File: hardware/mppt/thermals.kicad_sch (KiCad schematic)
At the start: 35 parts, among them J401 Conn_01x02, J402 Conn_01x03, J403 Conn_01x03, J404 Conn_01x03, Q401 Q_NMOS_GDS, U401 MCP9700Ax-ELT

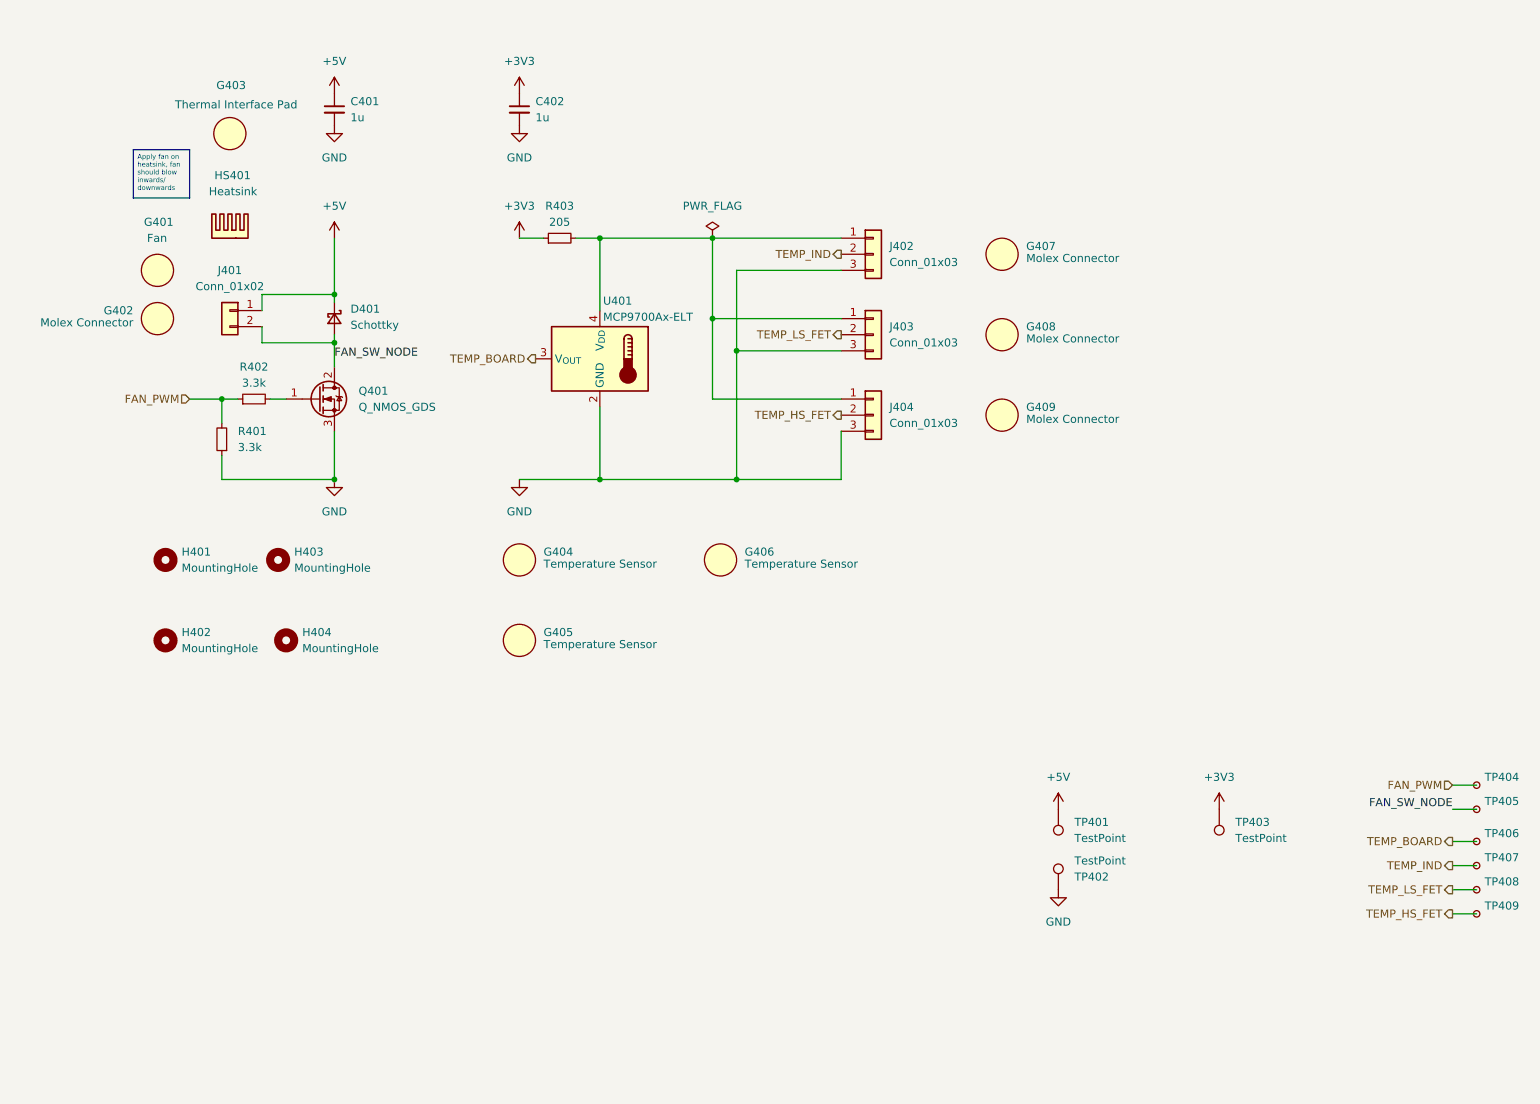
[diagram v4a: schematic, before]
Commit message: PCB variant for power regulation breakout.
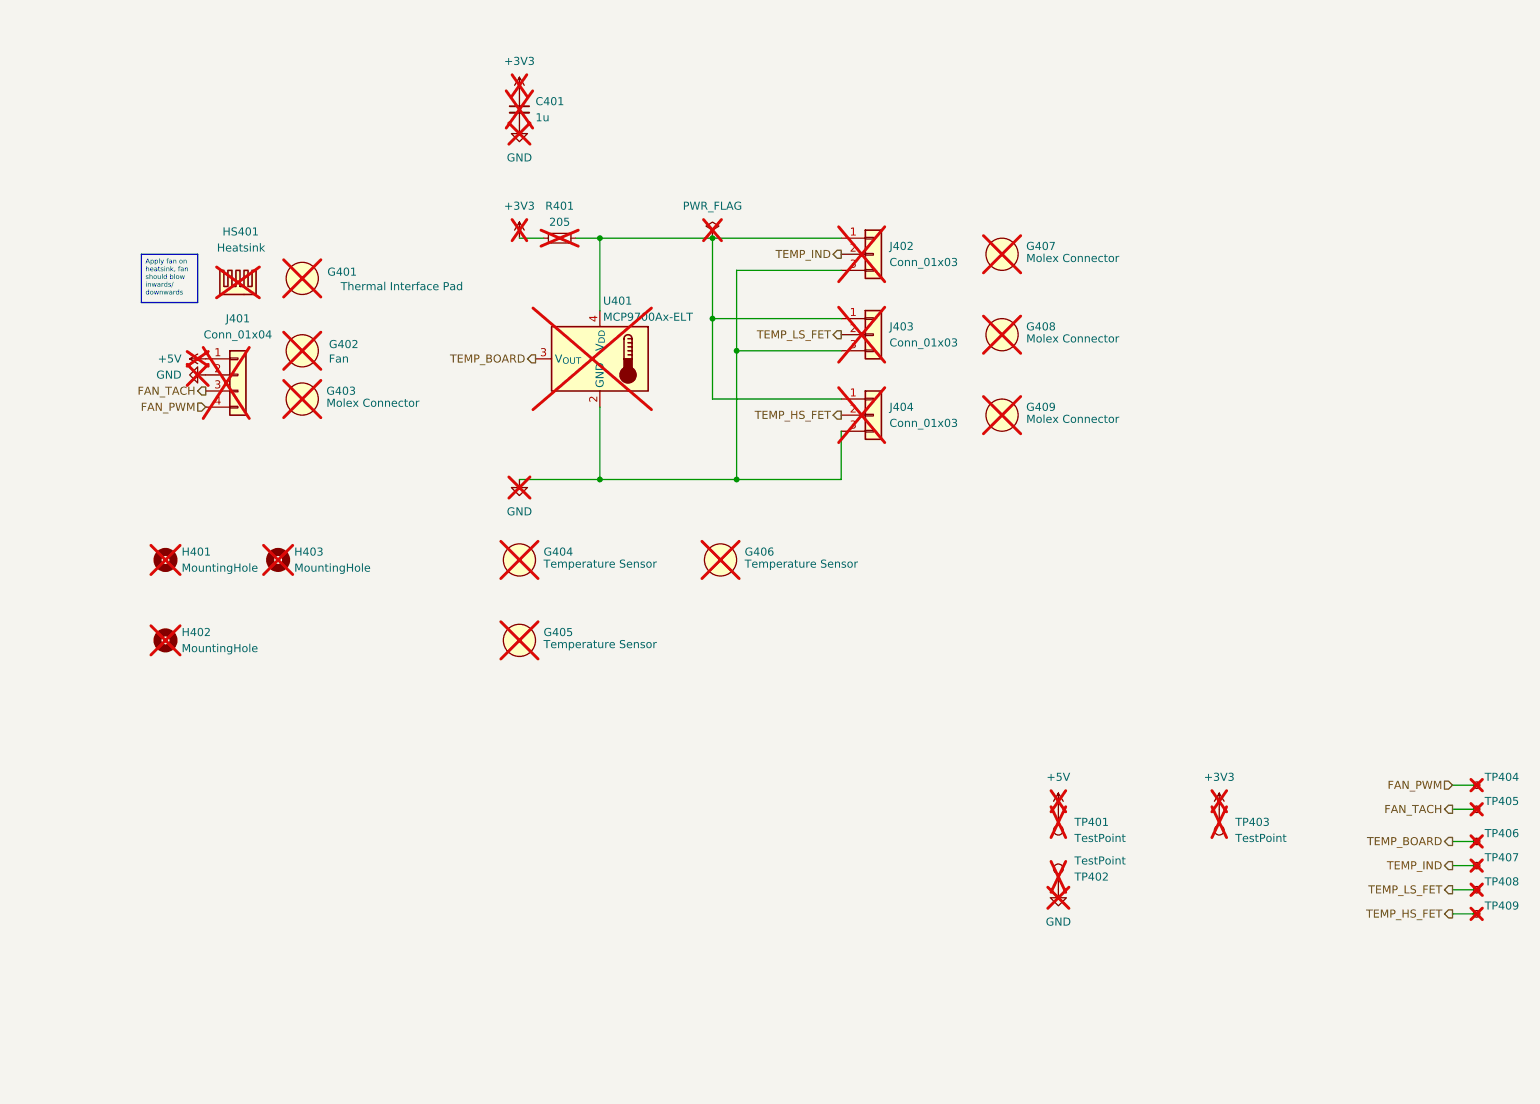
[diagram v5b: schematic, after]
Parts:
- removed C401: 1u, Capacitor_SMD:C_0603_1608Metric_Pad1.08x0.95mm_HandSolder, symbol Device:C_Small
- removed D401: Schottky, Diode_SMD:D_SOD-123F, symbol Device:D_Schottky_Small
- removed G402: Molex Connector, symbol generic_symbol:Generic_Symbol
- removed H404: MountingHole, MountingHole:MountingHole_2.7mm_M2.5, symbol Mechanical:MountingHole
- removed J401: Conn_01x02, Connector_Molex:Molex_Micro-Fit_3.0_43650-0215_1x02_P3.00mm_Vertical, symbol Connector_Generic:Conn_01x02
- removed Q401: Q_NMOS_GDS, Package_TO_SOT_SMD:SOT-223-3_TabPin2, symbol Device:Q_NMOS_GDS
- removed R401, R402: 3.3k, Resistor_SMD:R_0603_1608Metric_Pad0.98x0.95mm_HandSolder, symbol Device:R_Small
- added G403: Molex Connector, symbol generic_symbol:Generic_Symbol
- added J401: Conn_01x04, Connector_Molex:Molex_Micro-Fit_3.0_43650-0415_1x04_P3.00mm_Vertical, symbol Connector_Generic:Conn_01x04
- C401: renamed from C402; now not fitted; now left out of the parts list
- G401: renamed from G403; Distributor (none) -> Amazon; Manufacturer Wakefield Thermal -> OwlTree; Notes (none) -> https://www.amazon.com/gp/product/B096ZNHY8F/ref=sw_img_1?s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; P/N PL-2-3-254-H -> B096ZNHY8F; now not fitted; now left out of the parts list
- G402: renamed from G401; Manufacturer Adafruit -> CUI Devices; P/N 4468 -> CFM-2010CF-060-066-22; now not fitted; now left out of the parts list
- G404, G405, G406, G407, G408, G409, J402, J403, J404, TP401, TP402, TP403, TP404, TP405, TP406, TP407, TP408, TP409, U401: now not fitted; now left out of the parts list
- H401, H402, H403: footprint MountingHole:MountingHole_2.7mm_M2.5 -> MountingHole:MountingHole_2.2mm_M2; Notes M2.5 Hole -> M2 Hole; now not fitted
- HS401: Manufacturer Wakefield Thermal -> CUI Devices; P/N 624-60AB -> HSB03-141406; now not fitted; now left out of the parts list
- R401: renamed from R403; now not fitted; now left out of the parts list
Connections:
- net +5V: now also J401.1 (Pin_1)
- net FAN_PWM: now also J401.4 (Pin_4)
- net GND: now also J401.2 (Pin_2)
- net FAN_SW_NODE renamed FAN_TACH
- net FAN_TACH: now also J401.3 (Pin_3)

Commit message: complete layout, drc, signaling optimizations and added dnp testpoints
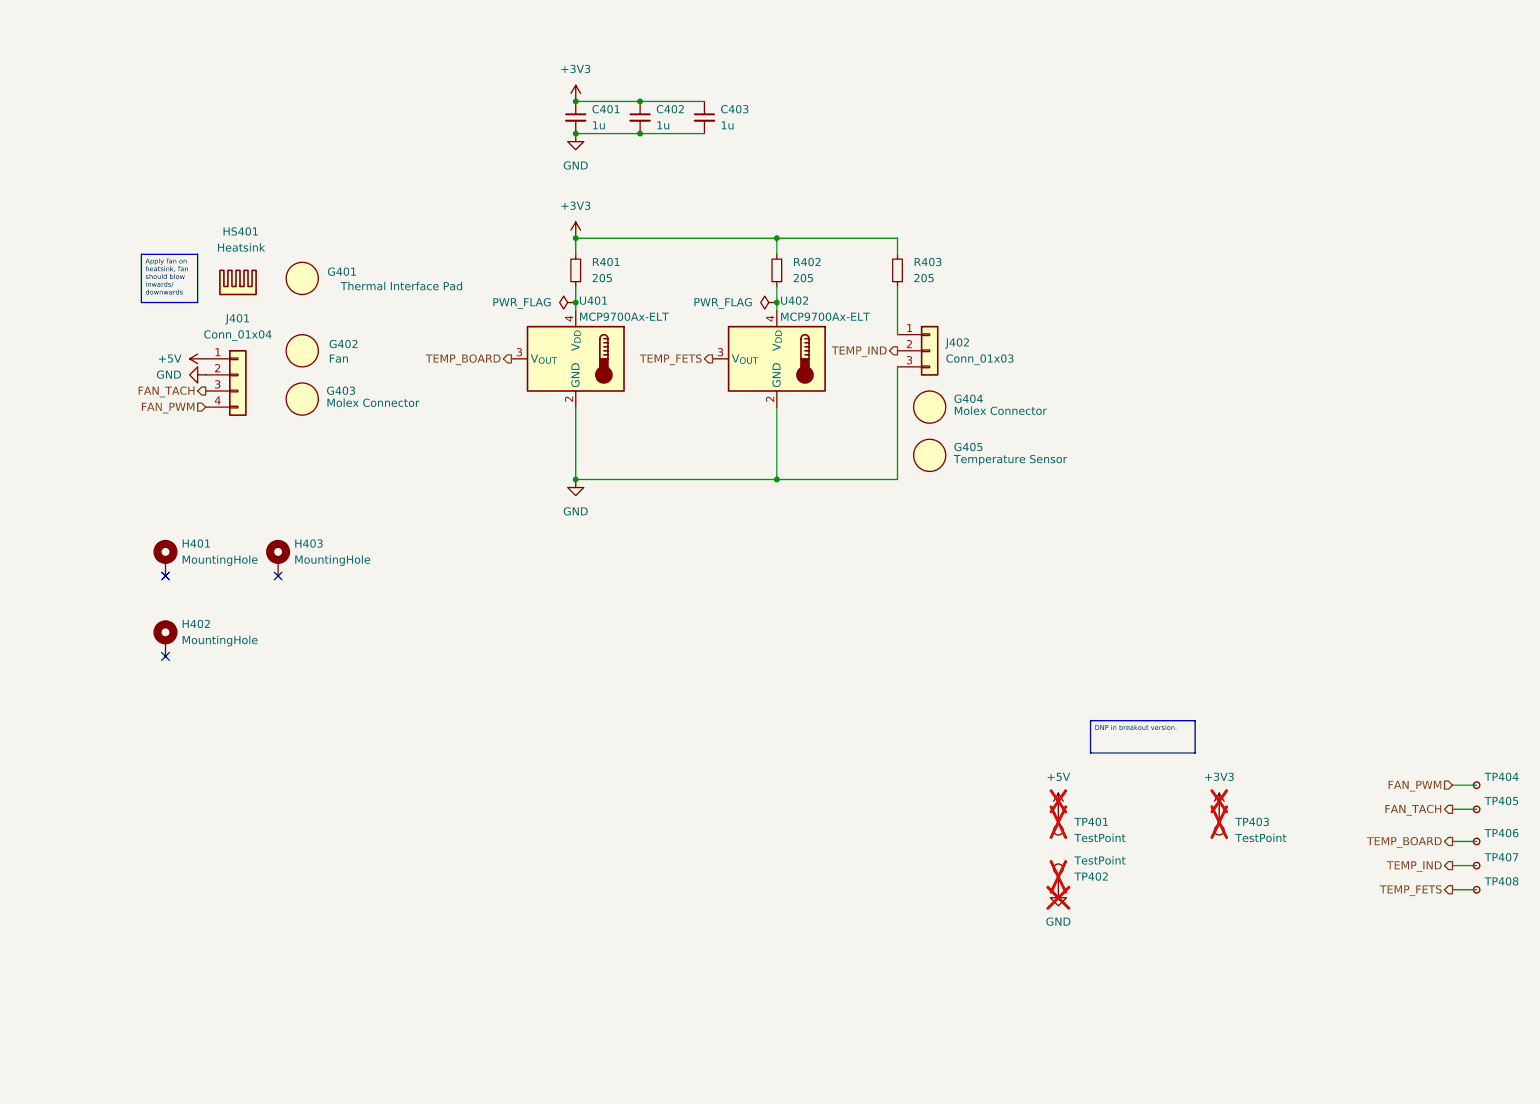
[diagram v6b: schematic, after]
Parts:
- removed G405, G406: Temperature Sensor, symbol generic_symbol:Generic_Symbol
- removed G408, G409: Molex Connector, symbol generic_symbol:Generic_Symbol
- removed J403, J404: Conn_01x03, Connector_Molex:Molex_Micro-Fit_3.0_43650-0315_1x03_P3.00mm_Vertical, symbol Connector_Generic:Conn_01x03
- removed TP409: TestPoint_Small, TestPoint:TestPoint_Pad_D1.0mm, symbol Connector:TestPoint_Small
- added C402, C403: 1u, Capacitor_SMD:C_0603_1608Metric_Pad1.08x0.95mm_HandSolder, symbol Device:C_Small
- added R402, R403: 205, Resistor_SMD:R_0603_1608Metric_Pad0.98x0.95mm_HandSolder, symbol Device:R_Small
- added U402: MCP9700Ax-ELT, Package_TO_SOT_SMD:SOT-353_SC-70-5, symbol Sensor_Temperature:MCP9700Ax-ELT
- C401, G401, G402, G403, HS401, J401, J402, R401, TP404, TP405, TP406, TP407, TP408, U401: now fitted; now in the parts list
- G404: renamed from G407; now fitted; now in the parts list
- G405: renamed from G404; now fitted; now in the parts list
- H401, H402, H403: footprint MountingHole:MountingHole_2.2mm_M2 -> MountingHole:MountingHole_2.2mm_M2_DIN965_Pad_TopBottom; symbol Mechanical:MountingHole -> Mechanical:MountingHole_Pad; now fitted
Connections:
- net +3V3: now also R401.2, C402.1, C403.1, R402.2, R403.2; no longer R401.1
- net GND: now also C402.2, C403.2, U402.2 (GND)
- net TEMP_LS_FET renamed TEMP_FETS
- net TEMP_FETS: now also U402.3 (V_{OUT})
- new net: R402.1, U402.4 (V_{DD})
- new net: R401.1, U401.4 (V_{DD})
- new net: J402.1 (Pin_1), R403.1
- no-connect marks 0 -> 3
